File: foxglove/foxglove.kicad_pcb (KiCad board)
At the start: 4 copper layers, 70.7 x 53.3 mm, 90 parts, among them J1 NEIGHBOR1, J2 NEIGHBOR2, J3 Conn_02x05_Odd_Even, J4 Conn_02x05_Odd_Even, J5 Conn_01x02_Female, J7 BONUS_ROW, U1 ICE40HX8K-CT256, U10 SHIFTER, U11 74HC4051, U12 SHIFTER, U13 74HC4051, U14 SHIFTER, U15 74HC4051, U16 SHIFTER, U17 74HC4051, U18 SHIFTER, U19 74HC4051, U2 TLV711, U20 SHIFTER, U21 74HC4051, U22 SHIFTER, U23 74HC4051, U24 SHIFTER, U3 MC4558CPT, U4 74LVC1G3157, U5 LM339, U6 ADP225, U7 DAC084S085, U8 74AHC1G04, U9 74HC4051

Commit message: Routed FPGA connections to J2 connector
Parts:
- C1, C2, C3, C4, R3, R6: moved to B.Cu
- moved C4 40.2 mm to (86.3, 152.0)
- moved C3 36.7 mm to (86.3, 151.1)
- moved R3 36.3 mm to (88.5, 148.6), turned to 90 degrees
- moved R6 35.7 mm to (87.8, 151.6), turned to 90 degrees
- moved C1 32.2 mm to (87.0, 149.1)
- moved C2 29.3 mm to (87.0, 148.1)
- moved U1 17.4 mm to (128.5, 95.0), turned to 0 degrees
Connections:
- net Net-(R7-Pad1) renamed /ADC_sel
- J1 pad 31: (no net) -> /J1.31
- U1 pad A1: /J2.34 -> /B3
- U1 pad A10: /J2.07 -> /J2.22
- U1 pad A11: /J2.08 -> /J2.19
- U1 pad A15: (no net) -> /J2.30
- U1 pad A16: /B8 -> /J2.29
- U1 pad A2: /J2.32 -> (no net)
- U1 pad A5: /J2.28 -> /J2.04
- U1 pad A6: /J2.26 -> /J2.06
- U1 pad A7: /J2.20 -> /J2.07
- U1 pad A9: /J2.13 -> /J2.18
- U1 pad B10: /J2.04 -> /J2.20
- U1 pad B11: (no net) -> /J2.17
- U1 pad B12: /J2.03 -> /J2.24
- U1 pad B13: (no net) -> /J2.26
- U1 pad B14: /B4 -> /J2.28
- U1 pad B15: /B2 -> /J2.35
- U1 pad B3: /J2.36 -> /B4
- U1 pad B4: /J2.31 -> (no net)
- U1 pad B5: /J2.29 -> (no net)
- U1 pad B6: /J2.23 -> /J2.03
- U1 pad B7: /J2.22 -> (no net)
- U1 pad B8: /J2.19 -> /J2.09
- U1 pad B9: /J2.17 -> /J2.15
- U1 pad C10: /J2.06 -> /J2.25
- U1 pad C11: (no net) -> /J2.32
- U1 pad C12: /B5 -> /J2.31
- U1 pad C13: /B7 -> /J2.34
- U1 pad C14: /B1 -> /J2.27
- U1 pad C15: Net-(U1-PadC15) -> VCC
- U1 pad C3: /J2.40 -> /B5
- U1 pad C4: /J2.35 -> /B2
- U1 pad C6: /J2.24 -> /J2.08
- U1 pad C7: /J2.21 -> /J2.11
- U1 pad C8: /J2.15 -> /J2.16
- U1 pad C9: /J2.10 -> /J2.21
- U1 pad D10: /J2.09 -> /J2.33
- U1 pad D11: (no net) -> /J2.36
- U1 pad D13: /B3 -> (no net)
- U1 pad D3: /J2.39 -> /B6
- U1 pad D4: /J2.37 -> /B7
- U1 pad D5: /J2.33 -> /B1
- U1 pad D6: /J2.27 -> /J2.10
- U1 pad D7: /J2.25 -> /J2.12
- U1 pad D8: /J2.18 -> /J2.13
- U1 pad D9: /J2.12 -> /J2.23
- U1 pad E1: Net-(U1-PadE1) -> VCC
- U1 pad E10: (no net) -> /J2.37
- U1 pad E11: /B6 -> /J2.40
- U1 pad E5: /J2.38 -> /B8
- U1 pad E6: /J2.30 -> (no net)
- U1 pad E9: /J2.11 -> /J2.38
- U1 pad F7: /J2.16 -> /J2.14
- U1 pad F9: /J2.14 -> /J2.39
- U1 pad G6: Net-(U1-PadE1) -> VCC
- U1 pad H10: Net-(U1-PadC15) -> VCC
- U1 pad H15: Net-(U1-PadC15) -> VCC
- U1 pad J6: Net-(U1-PadE1) -> VCC
- U1 pad K11: /J1.04 -> /J1.35
- U1 pad K9: /J1.21 -> /J1.18
- U1 pad L10: /J1.18 -> /J1.21
- U1 pad L11: /J1.08 -> /J1.31
- U1 pad L9: /J1.29 -> /J1.10
- U1 pad M11: /J1.11 -> /J1.28
- U1 pad M12: /J1.06 -> /J1.33
- U1 pad M8: /J1.35 -> /J1.05
- U1 pad M9: /J1.23 -> /J1.16
- U1 pad N1: Net-(U1-PadE1) -> VCC
- U1 pad N10: /J1.16 -> /J1.23
- U1 pad N12: /J1.09 -> /J1.30
- U1 pad N15: Net-(U1-PadC15) -> VCC
- U1 pad N7: (no net) -> /J1.03
- U1 pad N9: /J1.25 -> /J1.14
- U1 pad P10: /J1.17 -> /J1.22
- U1 pad P13: /J1.03 -> /J1.36
- U1 pad P6: /J1.36 -> /J1.04
- U1 pad P7: /J1.26 -> /J1.13
- U1 pad P8: /J1.32 -> /J1.08
- U1 pad P9: /J1.20 -> /J1.19
- U1 pad R10: /J1.19 -> /J1.20
- U1 pad R16: /J1.05 -> /J1.34
- U1 pad R6: /J1.33 -> /J1.07
- U1 pad R9: /J1.22 -> /J1.17
- U1 pad T10: /J1.15 -> /J1.24
- U1 pad T11: /J1.14 -> /J1.25
- U1 pad T13: /J1.10 -> /J1.29
- U1 pad T14: /J1.12 -> /J1.27
- U1 pad T15: /J1.13 -> /J1.26
- U1 pad T16: /J1.07 -> /J1.32
- U1 pad T5: /J1.34 -> /J1.06
- U1 pad T6: /J1.30 -> /J1.09
- U1 pad T7: /J1.28 -> /J1.11
- U1 pad T8: /J1.27 -> /J1.12
- U1 pad T9: /J1.24 -> /J1.15
- U7 pad 11: (no net) -> GND
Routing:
- net /J2.38: track 0.00 -> 55.6 mm, vias 0 -> 1
- net /J2.40: track 0.00 -> 55.5 mm, vias 0 -> 2
- net /J2.39: track 0.00 -> 54.7 mm, vias 0 -> 1
- net /J2.37: track 0.00 -> 51.5 mm, vias 0 -> 1
- net /J2.36: track 0.00 -> 50.4 mm, vias 0 -> 1
- net /J2.33: track 0.00 -> 46.8 mm, vias 0 -> 1
- net /J2.34: track 0.00 -> 45.9 mm, vias 0 -> 1
- net /J2.32: track 0.00 -> 45.0 mm, vias 0 -> 1
- net /J2.31: track 0.00 -> 44.4 mm, vias 0 -> 1
- net /J2.35: track 0.00 -> 44.1 mm
- net /J2.14: track 0.00 -> 40.5 mm, vias 0 -> 1
- net /J2.13: track 0.00 -> 38.4 mm, vias 0 -> 2
- net /J2.30: track 0.00 -> 36.2 mm
- net /J2.25: track 0.00 -> 35.8 mm, vias 0 -> 1
- net /J2.28: track 0.00 -> 35.7 mm
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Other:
- net class Default: clearance 0.1524 -> 0.127; trace_width 0.2032 -> 0.127; via_dia 0.762 -> 0.4572; via_drill 0.3302 -> 0.254
- rule pad_to_mask_clearance: 0.127 -> 0.0508
- rule trace_clearance: 0.1524 -> 0.127
- rule trace_min: 0.2032 -> 0.127
- rule via_min_drill: 0.3302 -> 0.254
- rule via_min_size: 0.6858 -> 0.4572

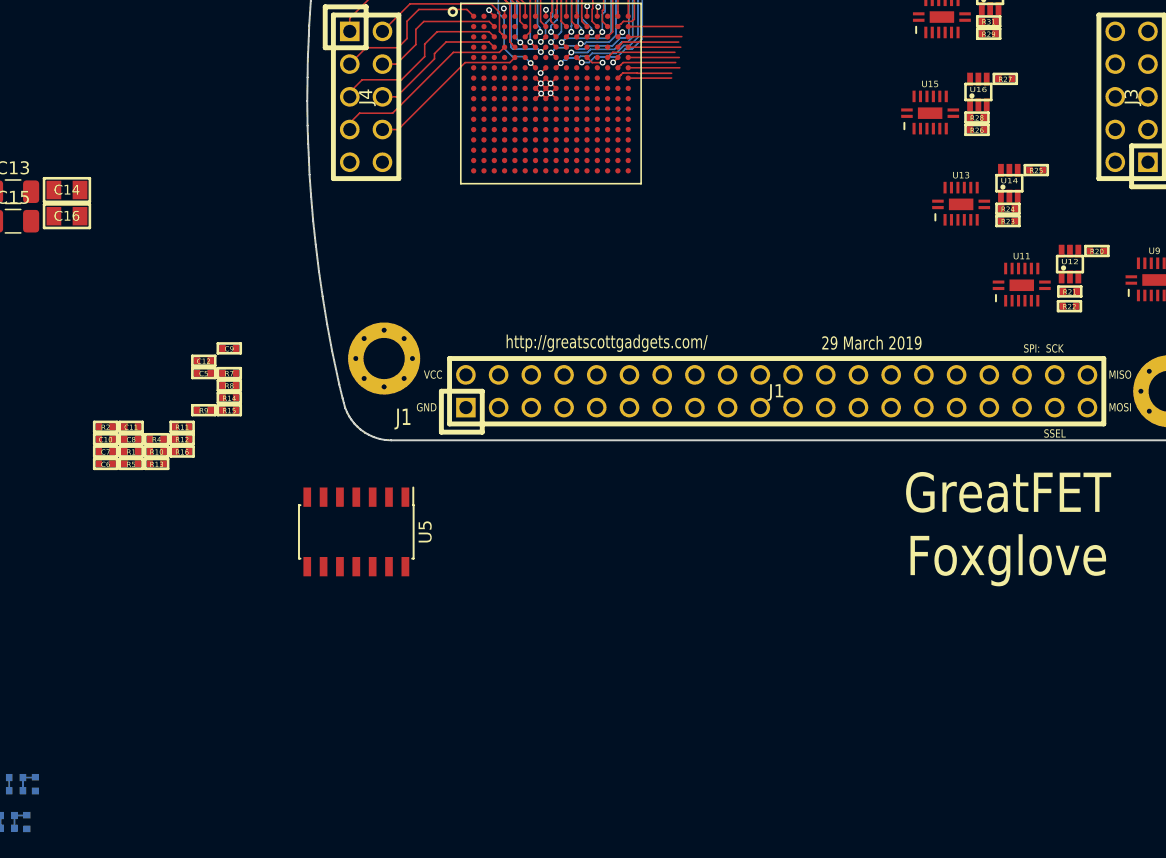
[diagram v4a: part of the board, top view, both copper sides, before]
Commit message: Foxglove: Routed FPGA to J1 header
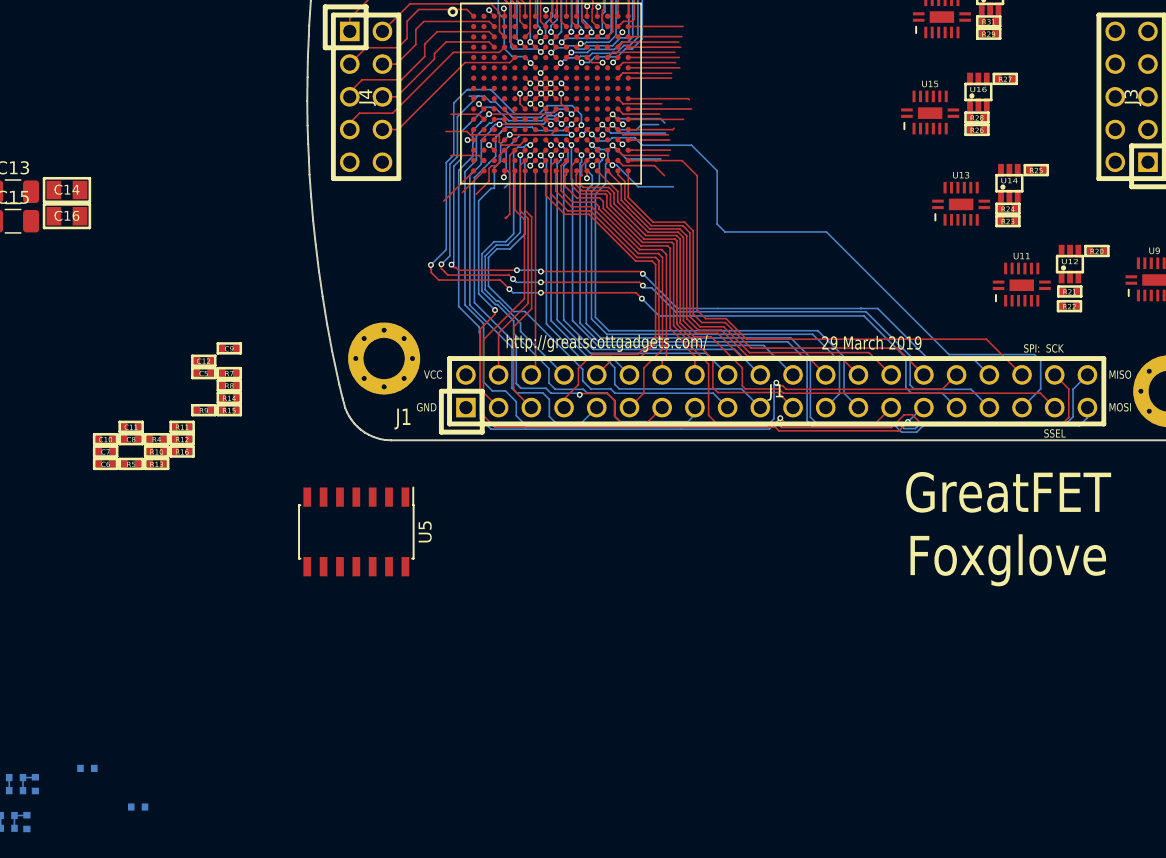
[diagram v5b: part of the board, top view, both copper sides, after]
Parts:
- R1, R2: moved to B.Cu
- moved R2 29.6 mm to (96.5, 150.4)
- moved R1 24.8 mm to (92.5, 147.4)
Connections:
- U1 pad K11: /J1.35 -> /J1.33
- U1 pad K9: /J1.18 -> /J1.27
- U1 pad L10: /J1.21 -> /J1.32
- U1 pad L11: /J1.31 -> /J1.13
- U1 pad L9: /J1.10 -> /J1.34
- U1 pad M11: /J1.28 -> /J1.31
- U1 pad M12: /J1.33 -> /J1.35
- U1 pad M8: /J1.05 -> /J1.09
- U1 pad M9: /J1.16 -> /J1.29
- U1 pad N10: /J1.23 -> /J1.22
- U1 pad N12: /J1.30 -> /J1.25
- U1 pad N7: /J1.03 -> /J1.15
- U1 pad N9: /J1.14 -> /J1.20
- U1 pad P10: /J1.22 -> /J1.18
- U1 pad P13: /J1.36 -> /J1.23
- U1 pad P6: /J1.04 -> /J1.08
- U1 pad P7: /J1.13 -> /J1.17
- U1 pad P8: /J1.08 -> /J1.19
- U1 pad P9: /J1.19 -> /J1.12
- U1 pad R10: /J1.20 -> /J1.14
- U1 pad R16: /J1.34 -> /J1.36
- U1 pad R6: /J1.07 -> /J1.04
- U1 pad R9: /J1.17 -> /J1.10
- U1 pad T10: /J1.24 -> /J1.16
- U1 pad T11: /J1.25 -> /J1.21
- U1 pad T13: /J1.29 -> /J1.24
- U1 pad T14: /J1.27 -> /J1.26
- U1 pad T15: /J1.26 -> /J1.28
- U1 pad T16: /J1.32 -> /J1.30
- U1 pad T5: /J1.06 -> /J1.03
- U1 pad T6: /J1.09 -> /J1.05
- U1 pad T7: /J1.11 -> /J1.06
- U1 pad T8: /J1.12 -> /J1.07
- U1 pad T9: /J1.15 -> /J1.11
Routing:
- net /J1.31: track 0.00 -> 73.6 mm, vias 0 -> 5
- net /J1.33: track 0.00 -> 72.6 mm, vias 0 -> 5
- net /J1.32: track 0.00 -> 70.6 mm, vias 0 -> 2
- net /J1.34: track 0.00 -> 65.7 mm, vias 0 -> 5
- net /J1.27: track 0.00 -> 64.1 mm, vias 0 -> 2
- net /J1.29: track 0.00 -> 63.3 mm, vias 0 -> 3
- net /MISO: track 0.00 -> 62.2 mm, vias 0 -> 1
- net /MOSI: track 0.00 -> 60.5 mm, vias 0 -> 1
- net /SCK: track 0.00 -> 59.9 mm
- net /SSEL: track 0.00 -> 51.2 mm
- net /J1.35: track 0.00 -> 49.5 mm, vias 0 -> 1
- net /J1.36: track 0.00 -> 43.7 mm
- net /J1.13: track 0.00 -> 42.5 mm, vias 0 -> 2
- net /J1.25: track 0.00 -> 40.2 mm, vias 0 -> 1
- net /J1.23: track 0.00 -> 38.3 mm, vias 0 -> 1
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
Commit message: Routed FPGA power and JTAG connections
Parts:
- added IC1: LFE5U-12F-6BG256C, gsg-modules:BGA256C80P16X16_1400X1400X170, F.Cu at (201.3, 131.7)
- added R41: 25k, gsg-modules:0402, F.Cu at (210.3, 124.1)
- added R42: 100k, gsg-modules:0402, F.Cu at (210.3, 125.1)
- added R43: 100k, gsg-modules:0402, F.Cu at (212.3, 124.1)
- added R44: 120k, gsg-modules:0402, F.Cu at (210.3, 126.0)
- added R45: 10k, gsg-modules:0402, F.Cu at (212.3, 125.1)
- added R46: R, gsg-modules:0402, F.Cu at (210.3, 127.0)
- added R47: R, gsg-modules:0402, F.Cu at (214.2, 124.1)
- added R48: 0, gsg-modules:0402, F.Cu at (194.2, 143.6)
- added R49: 0, gsg-modules:0402, F.Cu at (226.5, 124.1)
- added R50: 0, gsg-modules:0402, F.Cu at (199.3, 143.6)
- added R51: 0, gsg-modules:0402, F.Cu at (226.5, 128.3)
- added R52: 0, gsg-modules:0402, F.Cu at (204.3, 143.6)
- added R53: 0, gsg-modules:0402, F.Cu at (231.5, 124.1)
- added R54: 0, gsg-modules:0402, F.Cu at (209.3, 143.6)
- added R55: 0, gsg-modules:0402, F.Cu at (226.5, 132.4)
- U2: value TLV711 -> ADP225; footprint Package_SON:WSON-6_1.5x1.5mm_P0.5mm -> Package_CSP:LFCSP-8_2x2mm_P0.5mm
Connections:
- C10 pad 1: /DAC2 -> /A1
- C5 pad 1: +5V -> +2V5
- C6 pad 1: +2V5 -> +5V
- C7 pad 1: +1V2 -> +1V1
- J3 pad 2: /A2 -> /A1
- J3 pad 3: /A3 -> /A1
- J3 pad 4: /A4 -> /A1
- J3 pad 5: /A5 -> /A1
- J3 pad 6: /A6 -> /A1
- J3 pad 7: /A7 -> /A1
- J3 pad 8: /A8 -> /A1
- R11 pad 1: /DAC2 -> /A1
- U10 pad 4: Net-(U10-Pad4) -> /sheet5CF421BE/A_FPGA
- U11 pad 1: /DAC2 -> /ADC_A
- U11 pad 12: /ADC_A -> /VCCA
- U11 pad 15: Net-(U11-Pad15) -> GND
- U11 pad 2: /COMP1 -> /DAC3
- U11 pad 3: /A2 -> /sheet5D17D613/A_FPGA
- U11 pad 4: /COMP2 -> /COMP1
- U11 pad 5: /DAC3 -> /A1
- U12 pad 4: Net-(U11-Pad15) -> /sheet5D17D613/A_FPGA
- U13 pad 1: /DAC2 -> /ADC_A
- U13 pad 12: /ADC_A -> /VCCA
- U13 pad 15: Net-(U13-Pad15) -> GND
- U13 pad 2: /COMP1 -> /DAC3
- U13 pad 3: /A3 -> /sheet5D190CFC/A_FPGA
- U13 pad 4: /COMP2 -> /COMP1
- U13 pad 5: /DAC3 -> /A1
- U14 pad 4: Net-(U13-Pad15) -> /sheet5D190CFC/A_FPGA
- U15 pad 1: /DAC2 -> /ADC_A
- U15 pad 12: /ADC_A -> /VCCA
- U15 pad 15: Net-(U15-Pad15) -> GND
- U15 pad 2: /COMP1 -> /DAC3
- U15 pad 3: /A4 -> /sheet5D190CFD/A_FPGA
- U15 pad 4: /COMP2 -> /COMP1
- U15 pad 5: /DAC3 -> /A1
- U16 pad 4: Net-(U15-Pad15) -> /sheet5D190CFD/A_FPGA
- U17 pad 1: /DAC2 -> /ADC_A
- U17 pad 12: /ADC_A -> /VCCA
- U17 pad 15: Net-(U17-Pad15) -> GND
- U17 pad 2: /COMP1 -> /DAC3
- U17 pad 3: /A5 -> /sheet5D1A4642/A_FPGA
- U17 pad 4: /COMP2 -> /COMP1
- U17 pad 5: /DAC3 -> /A1
- U18 pad 4: Net-(U17-Pad15) -> /sheet5D1A4642/A_FPGA
- U19 pad 1: /DAC2 -> /ADC_A
- U19 pad 12: /ADC_A -> /VCCA
- U19 pad 15: Net-(U19-Pad15) -> GND
- U19 pad 2: /COMP1 -> /DAC3
- U19 pad 3: /A6 -> /sheet5D1A4643/A_FPGA
- U19 pad 4: /COMP2 -> /COMP1
- U19 pad 5: /DAC3 -> /A1
- U2 pad 3: +5V -> GND
- U2 pad 4: GND -> Net-(R41-Pad1)
- U2 pad 6: +1V2 -> +5V
- U20 pad 4: Net-(U19-Pad15) -> /sheet5D1A4643/A_FPGA
- U21 pad 1: /DAC2 -> /ADC_A
- U21 pad 12: /ADC_A -> /VCCA
- U21 pad 15: Net-(U21-Pad15) -> GND
- U21 pad 2: /COMP1 -> /DAC3
- U21 pad 3: /A7 -> /sheet5D1A4644/A_FPGA
- U21 pad 4: /COMP2 -> /COMP1
- U21 pad 5: /DAC3 -> /A1
- U22 pad 4: Net-(U21-Pad15) -> /sheet5D1A4644/A_FPGA
- U23 pad 1: /DAC2 -> /ADC_A
- U23 pad 12: /ADC_A -> /VCCA
- U23 pad 15: Net-(U23-Pad15) -> GND
- U23 pad 2: /COMP1 -> /DAC3
- U23 pad 3: /A8 -> /sheet5D1A4645/A_FPGA
- U23 pad 4: /COMP2 -> /COMP1
- U23 pad 5: /DAC3 -> /A1
- U24 pad 4: Net-(U23-Pad15) -> /sheet5D1A4645/A_FPGA
- U5 pad 4: /DAC2 -> /A1
- U6 pad 5: /DAC2 -> /A1
- U9 pad 1: /DAC2 -> /ADC_A
- U9 pad 12: /ADC_A -> /VCCA
- U9 pad 15: Net-(U10-Pad4) -> GND
- U9 pad 2: /COMP1 -> /DAC3
- U9 pad 3: /A1 -> /sheet5CF421BE/A_FPGA
- U9 pad 4: /COMP2 -> /COMP1
- U9 pad 5: /DAC3 -> /A1
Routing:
- net /J2.35: track 44.1 -> 32.4 mm
- net /J2.29: track 33.3 -> 23.5 mm
- net /J2.24: track 31.8 -> 27.6 mm
- net /J2.28: track 35.7 -> 31.7 mm
- net /J2.26: track 33.8 -> 30.4 mm
- net /J2.27: track 35.4 -> 33.4 mm
- net /J2.18: track 26.1 -> 25.1 mm
